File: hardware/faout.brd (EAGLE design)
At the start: 100 x 70 mm, 114 parts, among them IC1 MT48LC64M4A2, Q1 12MHz, Q2 ASFL, U1 93C46B, U10 OPA2277UA/2K5E4, U11 DAC8811DGK, U12 MCP1700T-2502E/TT, U13 AD7980ARMZ, U14 ADR435ARZ, U2 LTC3419EMS, U3 FLASH-SPI-25XXSMD1, U4 6SLX9TQG144, U5 AD8220ARMZ, U6 REF102AU, U7 OPA2277UA/2K5E4, U8 DAC8811DGK, U9 REF102AU

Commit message: Reroute USB
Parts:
- moved L2 11.1 mm to (37.5, 64.1), flipped to the bottom, turned to 180 degrees
- moved C4 8.52 mm to (37.5, 62.2), flipped to the bottom, turned to 0 degrees
- moved C7 6.02 mm to (37.5, 60.3), flipped to the bottom, turned to 0 degrees
- moved USB1 1.91 mm to (26.7, 65.9)
- moved C6 0.95 mm to (29.8, 53.0)
- moved C8 0.95 mm to (31.8, 53.0)
- moved L1 0.95 mm to (27.9, 53.0)
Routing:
- net USB_DM: track 22.6 -> 17.3 mm
- net USB_DP: track 23.7 -> 19.3 mm
- net N$5: track 11.9 -> 8.63 mm, vias 0 -> 1
- net USB_GND: track 17.6 -> 19.5 mm
- net 1V2: track 88.9 -> 87.8 mm
- net GND: vias 118 -> 119

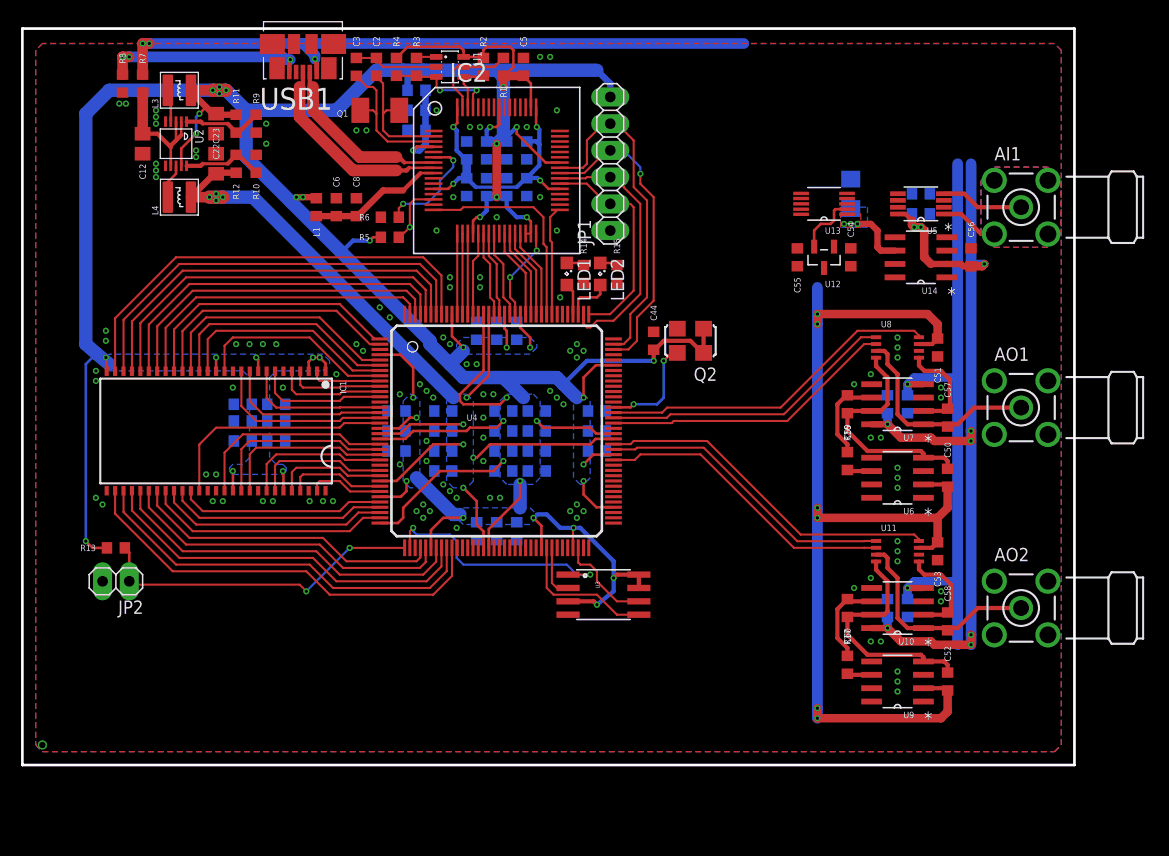
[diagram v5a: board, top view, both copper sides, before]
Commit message: Finalize USB and ADC layout.
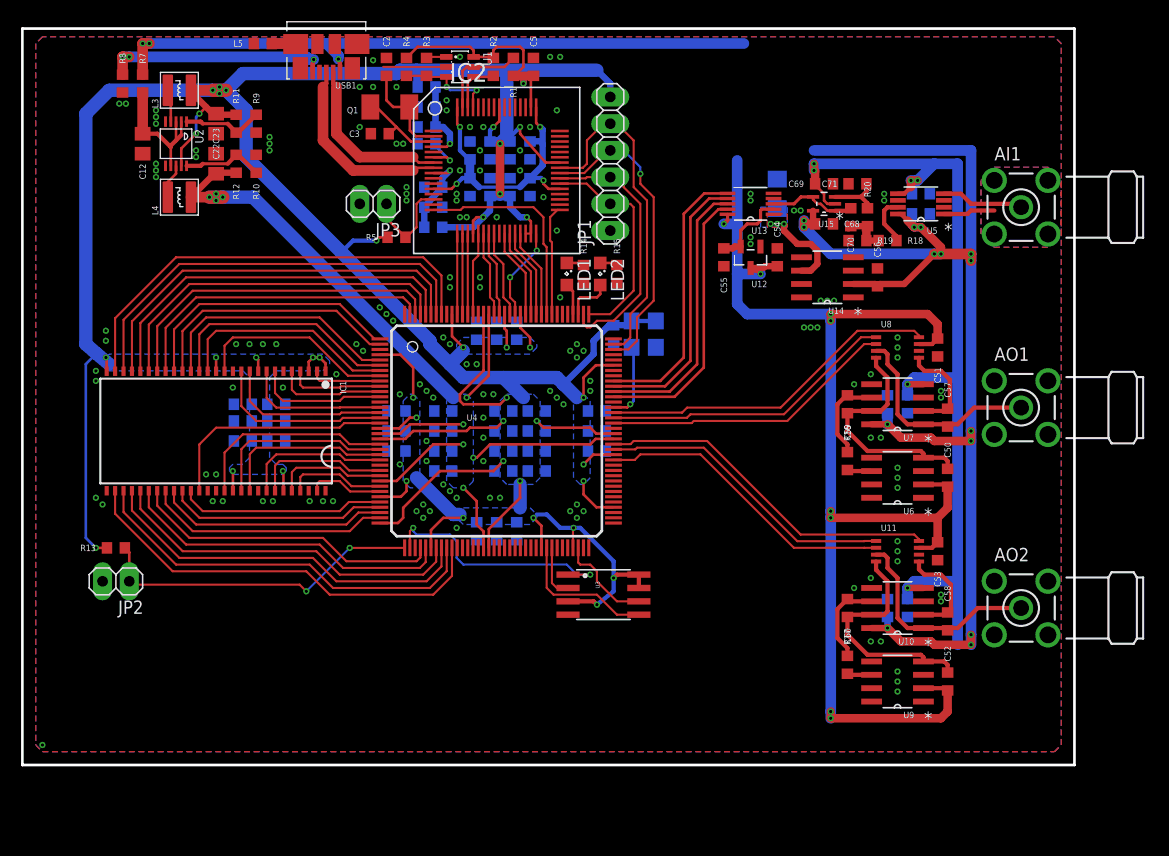
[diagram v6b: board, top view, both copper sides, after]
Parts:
- added C68, C69: 100nF, faout:R0603
- added C70: 114pF, faout:R0603
- added C71: 11.4pF, faout:R0603
- added JP3: (no value), pinhead:1X02
- added L5: (no value), faout:R0603
- added R18, R19: 7.47k, faout:R0603
- added R20: 134k, faout:R0603
- added U15: AD8627AKSZ-R2, faout:SOT65P210X110-5N
- moved L1 11.3 mm to (39.1, 51.1), flipped to the bottom, turned to 0 degrees
- moved C6 9.21 mm to (39.1, 53.0), flipped to the bottom, turned to 180 degrees
- moved C56 9.09 mm to (81.3, 46.4)
- moved U14 9.09 mm to (76.5, 46.4)
- moved R6 7.81 mm to (38.4, 59.1), flipped to the bottom, turned to 0 degrees
- moved C8 7.55 mm to (39.1, 54.9), flipped to the bottom, turned to 0 degrees
- moved C54 6.98 mm to (71.8, 48.3)
- moved C55 6.98 mm to (66.7, 48.3)
- moved C65 6.98 mm to (71.8, 54.3)
- moved U12 6.98 mm to (69.2, 48.3)
- moved U13 6.98 mm to (69.2, 53.3)
- moved C3 6.73 mm to (34.0, 60.0), turned to 180 degrees
- moved Q2 4.49 mm to (59.1, 41.0), flipped to the bottom, turned to 270 degrees
- moved C44 3.86 mm to (56.2, 41.0), flipped to the bottom, turned to 270 degrees
- moved USB1 2.22 mm to (28.9, 65.9)
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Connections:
- removed net +15V: C56.1, C61.1, C63.1, C66.1, U10.8, U14.2, U5.8, U7.8
- removed net -15V: C62.2, C64.2, C67.2, U10.4, U5.5, U7.4
- removed net VIO: U13.10
- new net A+12V: C56.1, C61.1, C63.1, C66.1, C68.1, U10.8, U14.2, U15.5, U5.8, U7.8
- new net A+3V3: C50.1, C51.1, C52.1, C53.1, C54.1, U11.7, U12.3, U13.10, U6.2, U8.7, U9.2
- new net A-12V: C62.2, C64.2, C67.2, C69.2, U10.4, U15.2, U5.5, U7.4
- new net N$13: R18.2, U5.7
- new net N$14: C70.2, R18.1, R19.2, R20.1
- new net N$15: C71.1, R20.2, U15.3
- new net N$16: L5.1, USB1.M6
- net !USB_RESET: now also JP3.1
- net 3V3: no longer C50.1, C51.1, C52.1, C53.1, U11.7, U6.2, U8.7, U9.2
- net ADC1_CNV: now also U4.100
- net ADC1_SCK: now also U4.98
- net ADC1_SDI: now also U4.97
- net ADC1_SDO: now also U4.99
- net GND: now also C68.2, C69.1, C71.2, JP3.2, L5.2, R19.1
- net N$12: now also C70.1, U13.3, U15.1, U15.4; no longer C54.1, U12.3
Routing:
- net A+12V: track 0.00 -> 125.2 mm, vias 0 -> 14
- net A+3V3: track 0.00 -> 121.7 mm, vias 0 -> 8
- net 3V3: track 499.5 -> 396.7 mm, vias 50 -> 41
- net A-12V: track 0.00 -> 87.2 mm, vias 0 -> 6
- net +15V: track 85.4 -> 0.00 mm, vias 9 -> 0
- net -15V: track 60.9 -> 0.00 mm, vias 2 -> 0
- net ADC1_SDO: track 0.00 -> 26.2 mm
- net ADC1_SCK: track 0.00 -> 26.2 mm
- net ADC1_SDI: track 0.00 -> 26.2 mm
- net ADC1_CNV: track 0.00 -> 26.2 mm
- net N$12: track 0.00 -> 8.41 mm
- net USB_REF: track 11.3 -> 3.94 mm, vias 2 -> 1
- net N$2: track 13.8 -> 8.37 mm
- net N$15: track 0.00 -> 5.26 mm
- net N$7: track 12.9 -> 8.01 mm, vias 0 -> 1
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
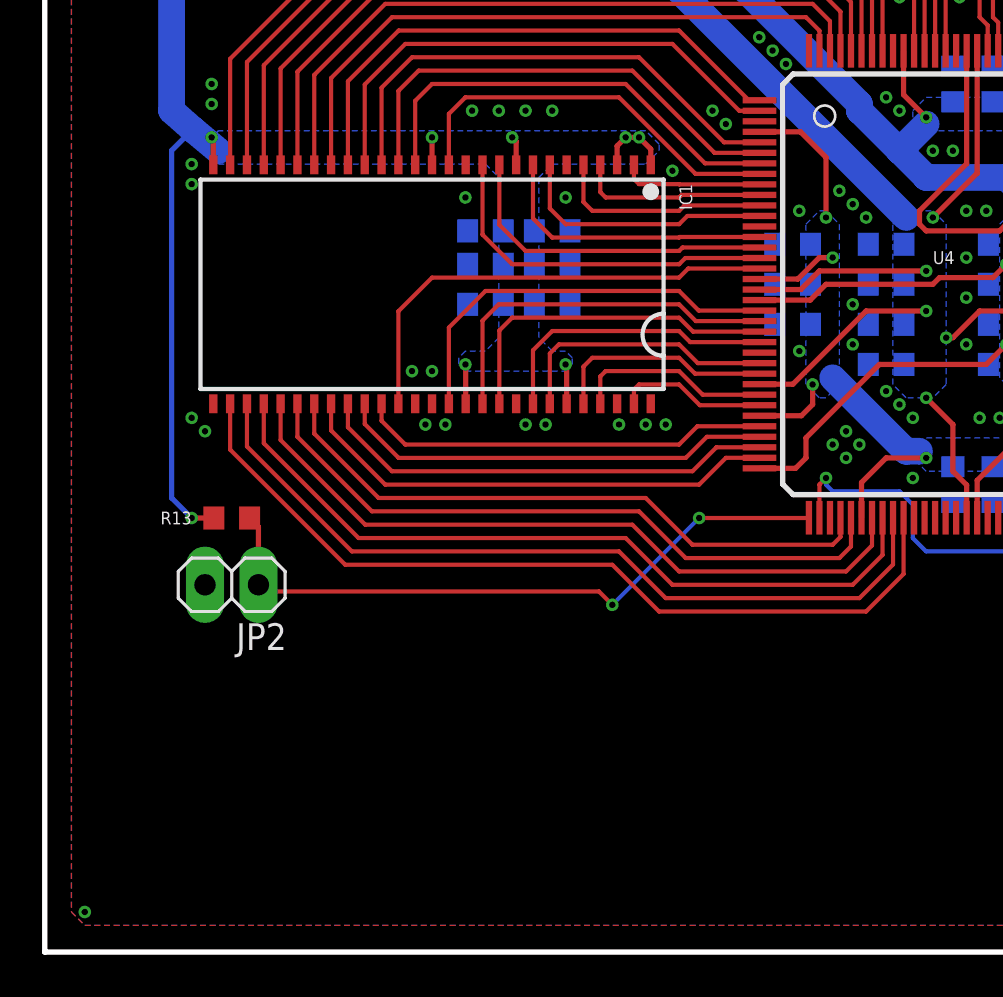
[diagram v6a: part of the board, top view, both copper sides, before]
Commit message: Added 7-segment display.
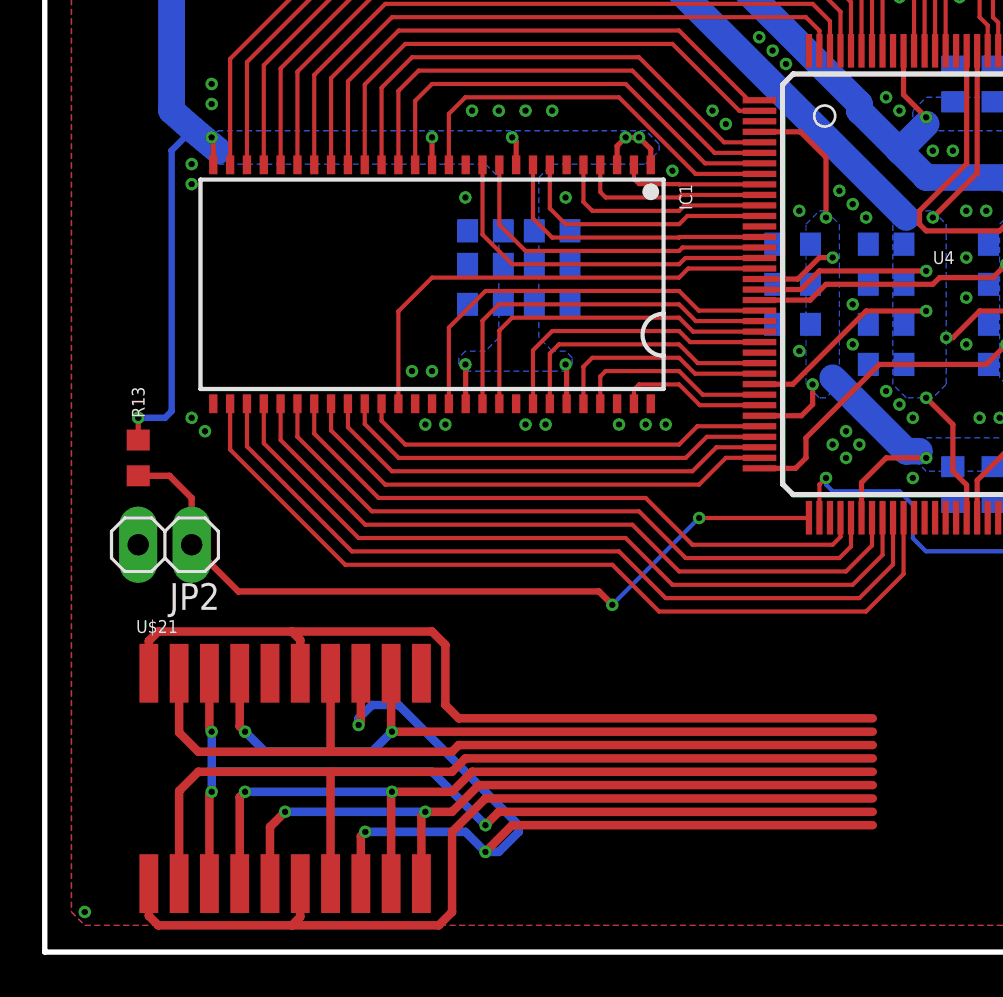
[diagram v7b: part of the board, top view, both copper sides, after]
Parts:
- added U$21: 7SEG_DISPLAY, faout:7SEG_DISPLAY
- moved R13 5.28 mm to (4.45, 23.5), turned to 90 degrees
- moved JP2 3.70 mm to (5.71, 19.4)
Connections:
- new net DISP_A: U$21.12, U$21.17
- new net DISP_B: U$21.11, U$21.16
- new net DISP_C: U$21.4, U$21.9
- new net DISP_CAT1: U$21.18, U$21.3
- new net DISP_CAT2: U$21.13, U$21.8
- new net DISP_D: U$21.2, U$21.7
- new net DISP_E: U$21.1, U$21.6
- new net DISP_F: U$21.14, U$21.19
- new net DISP_G: U$21.15, U$21.20
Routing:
- net DISP_F: track 0.00 -> 43.4 mm
- net DISP_G: track 0.00 -> 43.0 mm
- net DISP_CAT2: track 0.00 -> 43.0 mm, vias 0 -> 3
- net DISP_CAT1: track 0.00 -> 42.8 mm, vias 0 -> 3
- net DISP_E: track 0.00 -> 41.7 mm
- net DISP_D: track 0.00 -> 40.1 mm
- net DISP_A: track 0.00 -> 39.1 mm, vias 0 -> 2
- net DISP_C: track 0.00 -> 36.3 mm, vias 0 -> 2
- net DISP_B: track 0.00 -> 35.7 mm, vias 0 -> 2
- net RESET: track 31.6 -> 37.4 mm
- net 3V3: track 396.7 -> 393.0 mm

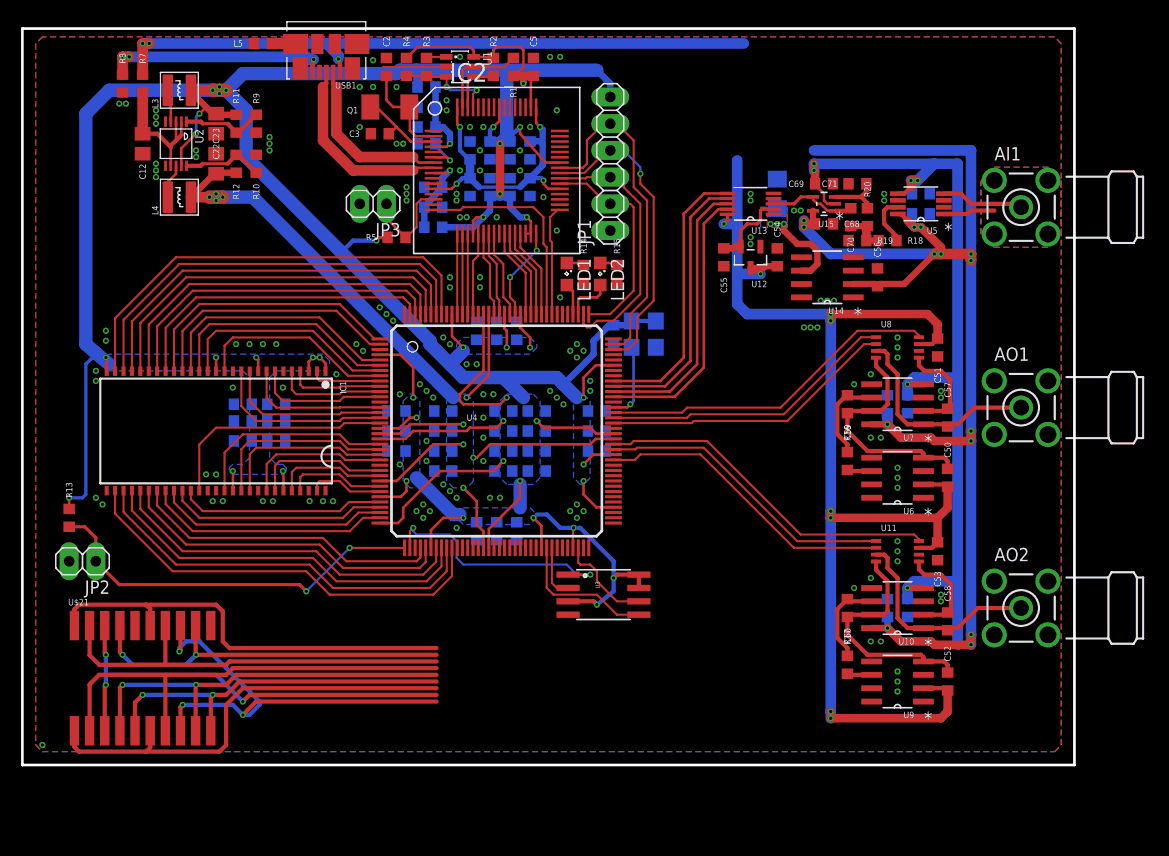
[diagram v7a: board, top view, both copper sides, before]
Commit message: Finished User IO, create new power supply.
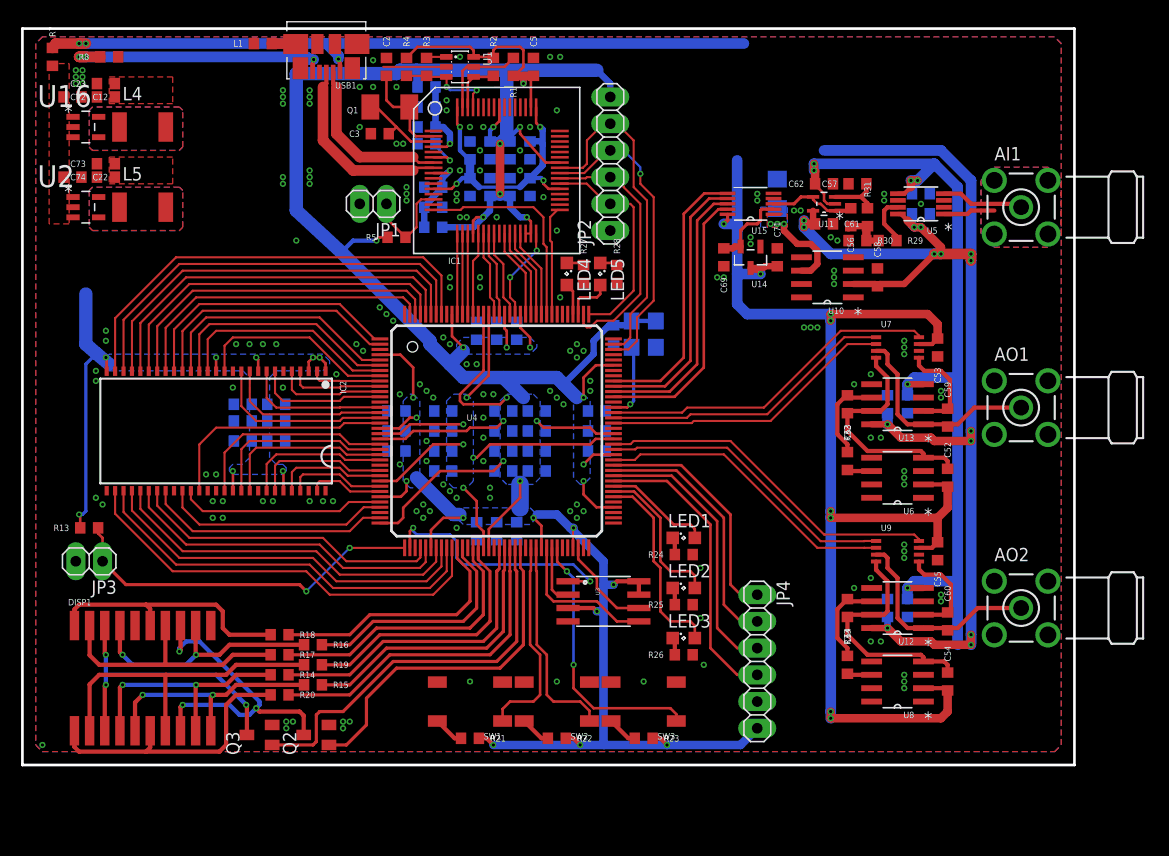
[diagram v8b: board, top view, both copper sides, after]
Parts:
- removed R10, R12, R9: 1K5 1%, faout:R0603
- removed R11: 6K8 1%, faout:R0603
- added C72, C73, C74: 4.7uF, faout:R0603
- added JP4: (no value), pinhead:1X06
- added LED3, LED4, LED5: (no value), led:SML0805
- added Q3: MUN2214T1, transistor-npn:SC59-BEC
- added Q4: ASFL, crystal:ASF
- added R21, R22, R23: 10k, faout:R0603
- added R24, R25, R26, R27, R28: 300, faout:R0603
- added R29, R30: 7.47k, faout:R0603
- added R31: 134k, faout:R0603
- added R32, R33: 2k, faout:R0603
- added SW1, SW2, SW3: SMD_TACT_SWITCH, faout:SMD_TACT_SWITCH
- added U16: LM3671MF-3.3, faout:SOT95P284X122-5N
- C12: value 10uF/10V -> 4.7uF; device faout:R0805 -> faout:R0603
- C22, C23: value 22uF/6V3 -> 4.7uF; device faout:R0805 -> faout:R0603
- C50: value 1uF? -> 100nF
- C54: value 1uF -> 1uF?
- C55: value 1uF -> 100nF
- C56: value 100nF -> 114pF
- C57: value 20pF -> 11.4pF
- C58: value 20pF -> 100nF
- C59, C60: value 1nF -> 20pF
- C63, C64: value 100nF -> 1nF
- C65: value 22uF -> 100nF; device resistor:C1206 -> faout:R0603
- C69: value 100nF -> 1uF
- C70: value 114pF -> 22uF; device faout:R0603 -> resistor:C1206
- C71: value 11.4pF -> 1uF
- IC1: value MT48LC64M4A2 -> (none); device faout:TSOP54-400 -> ftdichip-3:TQFP64-12X12
- IC2: value (none) -> MT48LC8M16A2; device ftdichip-3:TQFP64-12X12 -> faout:TSOP54-400
- JP1: device pinhead:1X06 -> pinhead:1X02
- JP2: device pinhead:1X02 -> pinhead:1X06
- L3: value 3.3uH -> (none); device Bogdan_Commons:VLS3015 -> faout:R0603
- L4: value 3.3uH -> 2.2uH; device Bogdan_Commons:VLS3015 -> rcl:L5038P
- L5: value (none) -> 2.2uH; device faout:R0603 -> rcl:L5038P
- Q2: value ASFL -> MUN2214T1; device crystal:ASF -> transistor-npn:SC59-BEC
- R14, R15: value 300 -> 100
- R16, R17: value 2k -> 100
- R18, R19: value 7.47k -> 100
- R20: value 134k -> 100
- U10: value OPA2277UA/2K5E4 -> ADR435ARZ
- U11: value DAC8811DGK -> AD8627AKSZ-R2; device faout:MSOP-8 -> faout:SOT65P210X110-5N
- U12: value MCP1700T-2502E/TT -> OPA2277UA/2K5E4; device faout:SOT95P264X112-3N -> faout:SOIC127P600X175-8N
- U13: value AD7980ARMZ -> OPA2277UA/2K5E4; device faout:SOP50P490X110-10N -> faout:SOIC127P600X175-8N
- U14: value ADR435ARZ -> MCP1700T-2502E/TT; device faout:SOIC127P600X175-8N -> faout:SOT95P264X112-3N
- U15: value AD8627AKSZ-R2 -> AD7980ARMZ; device faout:SOT65P210X110-5N -> faout:SOP50P490X110-10N
- U2: value LTC3419EMS -> LM3671MF-1.2; device Bogdan_Commons:MSOP10 -> faout:SOT95P284X122-5N
- U7: value OPA2277UA/2K5E4 -> DAC8811DGK; device faout:SOIC127P600X175-8N -> faout:MSOP-8
- U8: value DAC8811DGK -> REF102AU; device faout:MSOP-8 -> faout:SOIC127P600X175-8N
- U9: value REF102AU -> DAC8811DGK; device faout:SOIC127P600X175-8N -> faout:MSOP-8
- moved R20 72.0 mm to (24.4, 6.67), turned to 0 degrees
- moved R18 68.9 mm to (24.4, 12.4)
- moved R19 65.6 mm to (27.6, 9.53)
- moved JP2 62.8 mm to (55.9, 57.1), turned to 90 degrees
- moved R17 54.0 mm to (24.4, 10.5), turned to 0 degrees
- moved R16 53.7 mm to (27.6, 11.4), turned to 0 degrees
- moved Q2 49.2 mm to (27.9, 2.86), flipped to the top, turned to 90 degrees
- moved R15 48.6 mm to (27.6, 7.62), turned to 0 degrees
- moved R14 47.8 mm to (24.4, 8.57), turned to 0 degrees
- moved C54 43.5 mm to (87.9, 7.94)
- moved JP3 43.4 mm to (6.35, 19.4)
- moved C65 40.7 mm to (82.2, 14.9)
- moved C66 37.5 mm to (84.1, 14.9), turned to 90 degrees
- moved IC1 36.4 mm to (45.1, 56.5), turned to 270 degrees
- moved IC2 36.4 mm to (18.4, 31.8), turned to 180 degrees
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- renumbered U$21 to DISP1
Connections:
- removed net DISP_CAT2: DISP1.13, DISP1.8
- removed net FB_1V2: R10.2, R12.1, U2.10
- removed net FB_3V3: R11.1, R9.2, U2.1
- removed net LED_1: LED1.A, U4.112
- removed net LED_2: LED2.A, U4.111
- removed net RAM_A12: IC1.36, U4.34
- removed net SW_1V2: L4.1, U2.8
- removed net SW_3V3: L3.1, U2.4
- new net BUTTON1: SW1.1, U4.61
- new net BUTTON2: SW2.1, U4.62
- new net BUTTON3: SW3.1, U4.66
- new net DISP_EN1: Q3.B, U4.58
- new net DISP_EN2: Q2.B, U4.59
- new net DISP_INT_A: DISP1.12, DISP1.17, R14.1
- new net DISP_INT_B: DISP1.11, DISP1.16, R15.1
- new net DISP_INT_C: DISP1.4, DISP1.9, R16.1
- new net DISP_INT_D: DISP1.2, DISP1.7, R17.1
- new net DISP_INT_E: DISP1.1, DISP1.6, R18.1
- new net DISP_INT_F: DISP1.14, DISP1.19, R19.1
- new net DISP_INT_G: DISP1.15, DISP1.20, R20.1
- new net JP_1: JP4.1, U4.84
- new net JP_2: JP4.2, U4.83
- new net JP_3: JP4.3, U4.82
- new net JP_4: JP4.4, U4.81
- new net LED1: LED1.A, U4.80
- new net LED2: LED2.A, U4.79
- new net LED3: LED3.A, U4.78
- new net LED_4: LED4.A, U4.112
- new net LED_5: LED5.A, U4.111
- new net N$17: DISP1.13, DISP1.8, Q2.C
- new net N$18: R21.1, SW1.2
- new net N$19: R22.1, SW2.2
- new net N$20: R23.1, SW3.2
- new net N$21: LED1.C, R24.2
- new net N$22: LED2.C, R25.2
- new net N$23: LED3.C, R26.2
- new net N$24: L4.1, U16.5
- new net N$25: L5.1, U2.5
- net !DAC1_CS: now also U7.8; no longer U8.8
- net !DAC2_CS: now also U9.8; no longer U11.8
- net !RAM_CAS: now also IC2.17; no longer IC1.17
- net !RAM_RAS: now also IC2.18; no longer IC1.18
- net !RAM_WE: now also IC2.16; no longer IC1.16
- net !USB_OE: now also IC1.33; no longer IC2.33
- net !USB_RD: now also IC1.28; no longer IC2.28
- net !USB_RESET: now also IC1.14, JP1.1; no longer IC2.14, JP3.1
- net !USB_RXF: now also IC1.26; no longer IC2.26
- net !USB_TXE: now also IC1.27; no longer IC2.27
- net !USB_WR: now also IC1.29; no longer IC2.29
- net 1V2: now also C73.1, C74.1, L5.2, U2.4; no longer C23.1, L4.2, R12.2
- net 1V8: now also IC1.12, IC1.37, IC1.49, IC1.64; no longer IC2.12, IC2.37, IC2.49, IC2.64
- net 2V5: now also C69.1, U14.2, U15.2; no longer C55.1, U12.2, U13.2
- net 3V3: now also C23.1, C72.1, IC1.20, IC1.30, IC1.31, IC1.42, IC1.50, IC1.56, IC2.1, IC2.14, IC2.27, IC2.3, IC2.43, IC2.49, IC2.9, JP2.6, JP4.6, L3.1, L4.2, Q4.1, Q4.4, R21.2, R22.2, R23.2, U16.4, U2.3; no longer C22.1, IC1.1, IC1.14, IC1.27, IC1.3, IC1.43, IC1.49, IC1.9, IC2.20, IC2.30, IC2.31, IC2.42, IC2.50, IC2.56, JP1.6, L1.1, L3.2, Q2.1, Q2.4, R11.2, U2.9
- net 5V0: now also C22.1, U16.1, U16.3, U2.1; no longer U2.2, U2.3, U2.7
- net A+12V: now also C50.1, C58.1, C65.1, C67.1, U10.2, U11.5, U12.8, U13.8; no longer C56.1, C63.1, C66.1, C68.1, U10.8, U14.2, U15.5, U7.8
- net A+3V3: now also C55.1, C71.1, U14.3, U15.10, U7.7, U8.2, U9.7; no longer C50.1, C51.1, U11.7, U12.3, U13.10, U8.7, U9.2
- net A-12V: now also C51.2, C66.2, C68.2, U11.2, U12.4, U13.4; no longer C64.2, C67.2, C69.2, U10.4, U15.2, U7.4
- net ADC1_CNV: now also U15.6; no longer U13.6
- net ADC1_REF: now also C70.1, U10.6, U15.1; no longer C65.1, U13.1, U14.6
- net ADC1_SCK: now also U15.8; no longer U13.8
- net ADC1_SDI: now also U15.9; no longer U13.9
- net ADC1_SDO: now also U15.7; no longer U13.7
- net CLK_IN: now also Q4.3; no longer Q2.3
- net DAC1_CLK: now also U7.1; no longer U8.1
- net DAC1_IOUT: now also C59.2, U13.2, U7.5; no longer C57.2, U7.2, U8.5
- net DAC1_SDI: now also U7.2; no longer U8.2
- net DAC1_VOUT: now also C59.1, U13.1, U7.3; no longer C57.1, U7.1, U8.3
- net DAC1_VREF: now also C52.2, C63.2, U13.7, U7.4; no longer C50.2, C59.2, U7.7, U8.4
- net DAC1_VREFOUT: now also C63.1, R32.2, U13.6; no longer C59.1, R16.2, U7.6
- net DAC2_CLK: now also U9.1; no longer U11.1
- net DAC2_IOUT: now also C60.2, U12.2, U9.5; no longer C58.2, U10.2, U11.5
- net DAC2_SDI: now also U9.2; no longer U11.2
- net DAC2_VOUT: now also C60.1, U12.1, U9.3; no longer C58.1, U10.1, U11.3
- net DAC2_VREF: now also C54.2, C64.2, U12.7, U8.4; no longer C52.2, C60.2, U10.7, U11.4
- net DAC2_VREFOUT: now also C64.1, R33.2, U12.6; no longer C60.1, R17.2, U10.6
- net DISP_A: now also R14.2, U4.55; no longer DISP1.12, DISP1.17
- net DISP_B: now also R15.2, U4.56; no longer DISP1.11, DISP1.16
- net DISP_C: now also R16.2, U4.48; no longer DISP1.4, DISP1.9
- net DISP_CAT1: now also Q3.C
- net DISP_D: now also R17.2, U4.50; no longer DISP1.2, DISP1.7
- net DISP_E: now also R18.2, U4.47; no longer DISP1.1, DISP1.6
- net DISP_F: now also R19.2, U4.51; no longer DISP1.14, DISP1.19
- net DISP_G: now also R20.2, U4.57; no longer DISP1.15, DISP1.20
- net EECS: now also IC1.63; no longer IC2.63
- net EEDATA: now also IC1.61; no longer IC2.61
- net EESK: now also IC1.62; no longer IC2.62
- net GND: now also C50.2, C51.1, C57.2, C58.2, C66.1, C67.2, C68.1, C69.2, C70.2, C72.2, C73.2, C74.2, IC1.1, IC1.10, IC1.11, IC1.13, IC1.15, IC1.25, IC1.35, IC1.47, IC1.5, IC1.51, IC2.12, IC2.28, IC2.41, IC2.46, IC2.52, IC2.54, IC2.6, JP1.2, JP2.1, JP4.5, L1.2, Q2.E, Q3.E, Q4.2, R24.1, R25.1, R26.1, R27.1, R28.1, R30.1, SW1.3, SW1.4, SW2.3, SW2.4, SW3.3, SW3.4, U10.4, U12.3, U12.5, U13.3, U14.1, U15.4, U15.5, U16.2, U2.2, U7.6, U9.6; no longer C51.2, C54.2, C56.2, C63.2, C64.1, C66.2, C67.1, C68.2, C69.1, IC1.12, IC1.28, IC1.41, IC1.46, IC1.52, IC1.54, IC1.6, IC2.1, IC2.10, IC2.11, IC2.13, IC2.15, IC2.25, IC2.35, IC2.47, IC2.5, IC2.51, JP1.1, JP2.2, L5.2, Q2.2, R10.1, R14.1, R15.1, R19.1, R9.1, U10.3, U10.5, U11.6, U12.1, U13.4, U14.4, U2.5, U2.6, U7.3, U7.5, U8.6
- net N$1: now also IC1.2; no longer IC2.2
- net N$10: now also R32.1; no longer R16.1
- net N$12: now also C56.1, U11.1, U11.4, U15.3; no longer C70.1, U13.3, U15.1, U15.4
- net N$13: now also R29.2; no longer R18.2
- net N$14: now also C56.2, R29.1, R30.2, R31.1; no longer C70.2, R18.1, R19.2, R20.1
- net N$15: now also C57.1, R31.2, U11.3; no longer C71.1, R20.2, U15.3
- net N$16: now also L1.1; no longer L5.1
- net N$2: now also IC1.3; no longer IC2.3
- net N$3: now also LED4.C, R27.2; no longer LED1.C, R14.2
- net N$4: now also LED5.C, R28.2; no longer LED2.C, R15.2
- net N$5: now also IC1.4, L3.2; no longer IC2.4, L2.2
- net N$7: now also IC1.9, L2.2; no longer IC2.9, L1.2
- net N$8: now also R33.1, U8.6; no longer R17.1, U9.6
- net RAM_A0: now also IC2.23; no longer IC1.23
- net RAM_A1: now also IC2.24; no longer IC1.24
- net RAM_A10: now also IC2.22; no longer IC1.22
- net RAM_A11: now also IC2.35; no longer IC1.35
- net RAM_A2: now also IC2.25; no longer IC1.25
- net RAM_A3: now also IC2.26; no longer IC1.26
- net RAM_A4: now also IC2.29; no longer IC1.29
- net RAM_A5: now also IC2.30; no longer IC1.30
- net RAM_A6: now also IC2.31; no longer IC1.31
- net RAM_A7: now also IC2.32; no longer IC1.32
- net RAM_A8: now also IC2.33; no longer IC1.33
- net RAM_A9: now also IC2.34; no longer IC1.34
- net RAM_BA0: now also IC2.20; no longer IC1.20
- net RAM_BA1: now also IC2.21; no longer IC1.21
- net RAM_CKE: now also IC2.37; no longer IC1.37
- net RAM_CLK: now also IC2.38; no longer IC1.38
- net RAM_CS: now also IC2.19; no longer IC1.19
- net RAM_DQ0: now also IC2.2; no longer IC1.2
- net RAM_DQ1: now also IC2.4; no longer IC1.4
- net RAM_DQ10: now also IC2.45; no longer IC1.45
- net RAM_DQ11: now also IC2.47; no longer IC1.47
- net RAM_DQ12: now also IC2.48; no longer IC1.48
- net RAM_DQ13: now also IC2.50; no longer IC1.50
- net RAM_DQ14: now also IC2.51; no longer IC1.51
- net RAM_DQ15: now also IC2.53; no longer IC1.53
- net RAM_DQ2: now also IC2.5; no longer IC1.5
- net RAM_DQ3: now also IC2.7; no longer IC1.7
- net RAM_DQ4: now also IC2.8; no longer IC1.8
- net RAM_DQ5: now also IC2.10; no longer IC1.10
- net RAM_DQ6: now also IC2.11; no longer IC1.11
- net RAM_DQ7: now also IC2.13; no longer IC1.13
- net RAM_DQ8: now also IC2.42; no longer IC1.42
- net RAM_DQ9: now also IC2.44; no longer IC1.44
- net RAM_DQMH: now also IC2.39; no longer IC1.39
- net RAM_DQML: now also IC2.15; no longer IC1.15
- net RESET: now also JP3.1; no longer JP2.1
- net TCK: now also IC1.38, JP2.2; no longer IC2.38, JP1.2
- net TDI: now also IC1.39, JP2.3; no longer IC2.39, JP1.3
- net TDO: now also IC1.40, JP2.4; no longer IC2.40, JP1.4
- net TMS: now also IC1.41, JP2.5; no longer IC2.41, JP1.5
- net USB_CLKOUT: now also IC1.32; no longer IC2.32
- net USB_D0: now also IC1.16; no longer IC2.16
- net USB_D1: now also IC1.17; no longer IC2.17
- net USB_D2: now also IC1.18; no longer IC2.18
- net USB_D3: now also IC1.19; no longer IC2.19
- net USB_D4: now also IC1.21; no longer IC2.21
- net USB_D5: now also IC1.22; no longer IC2.22
- net USB_D6: now also IC1.23; no longer IC2.23
- net USB_D7: now also IC1.24; no longer IC2.24
- net USB_DM: now also IC1.7; no longer IC2.7
- net USB_DP: now also IC1.8; no longer IC2.8
- net USB_REF: now also IC1.6; no longer IC2.6
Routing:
- net DISP_CAT2: track 43.0 -> 0.00 mm, vias 3 -> 0
- net 1V2: track 87.8 -> 47.0 mm, vias 9 -> 5
- net DISP_EN1: track 0.00 -> 37.8 mm
- net DISP_EN2: track 0.00 -> 33.2 mm
- net DISP_INT_F: track 0.00 -> 30.9 mm
- net N$17: track 0.00 -> 30.7 mm, vias 0 -> 3
- net JP_4: track 0.00 -> 28.2 mm
- net DISP_INT_G: track 0.00 -> 27.0 mm
- net JP_3: track 0.00 -> 26.4 mm
- net BUTTON3: track 0.00 -> 25.4 mm, vias 0 -> 2
- net DISP_INT_E: track 0.00 -> 24.6 mm
- net DISP_INT_D: track 0.00 -> 24.6 mm
- net JP_2: track 0.00 -> 24.4 mm
- net DISP_INT_C: track 0.00 -> 24.1 mm, vias 0 -> 2
- net DISP_INT_A: track 0.00 -> 23.3 mm, vias 0 -> 2
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- added copper zone on layer 1, net 1V2
- added copper zone on layer 1, net 3V3
- added copper zone on layer 1, net 5V0
- added copper zone on layer 1, net N$26
- added copper zone on layer 16, net N$26
